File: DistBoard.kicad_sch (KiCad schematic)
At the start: 17 parts, among them J1 22-27-2021, J2 SSM-103-L-SV, J3 SSM-103-L-SV, J4 SSM-103-L-SV, J5 SSM-103-L-SV, U1 TLE2426CDR

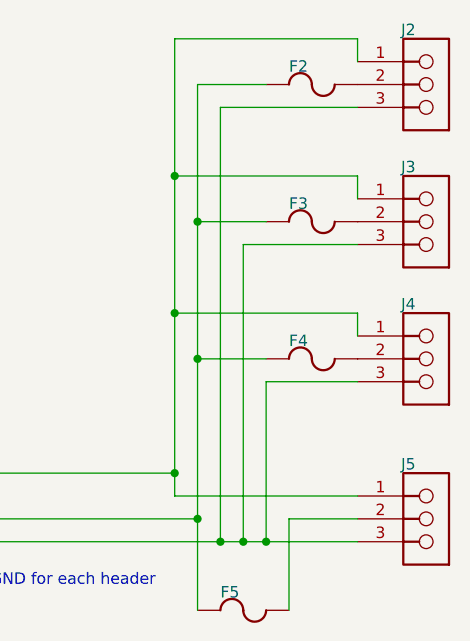
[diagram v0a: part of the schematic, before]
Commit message: Swap to through hole headers
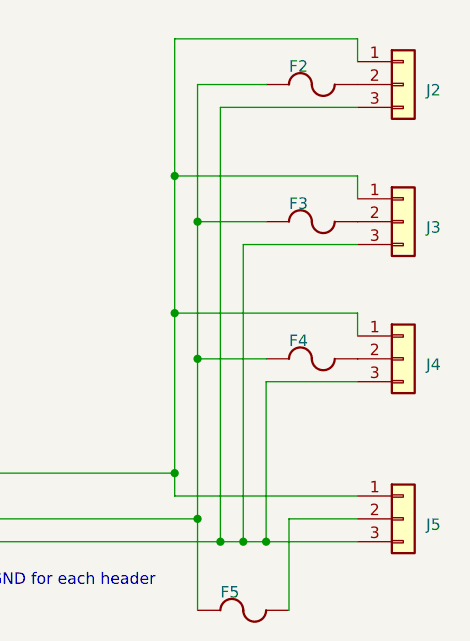
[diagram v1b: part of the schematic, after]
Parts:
- removed J2, J3, J4, J5: SSM-103-L-SV, SMTC-SSM-103-X-SV, symbol DistBoard-altium-import:root_3_SMTC-SSM-103-X-SV
- added J2, J3, J4, J5: Conn_01x03, Connector_PinHeader_2.54mm:PinHeader_1x03_P2.54mm_Vertical, symbol Connector_Generic:Conn_01x03
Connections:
- net AGND: now also J2.3 (Pin_3), J3.3 (Pin_3), J4.3 (Pin_3), J5.3 (Pin_3)
- net GND: now also J2.1 (Pin_1), J3.1 (Pin_1), J4.1 (Pin_1), J5.1 (Pin_1)
- net at F4.2: now also J4.2 (Pin_2)
- net at F5.2: now also J5.2 (Pin_2)
- net at F3.2: now also J3.2 (Pin_2)
- net at F2.2: now also J2.2 (Pin_2)

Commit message: Swap to socket headers and fix drc violations
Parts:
- J2, J3, J4, J5: footprint Connector_PinHeader_2.54mm:PinHeader_1x03_P2.54mm_Vertical -> Connector_PinSocket_2.54mm:PinSocket_1x03_P2.54mm_Vertical
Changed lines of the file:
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@@
       (effects (font (size 1.27 1.27)) (justify left) hide)
     )
-    (property "Footprint" "Connector_PinHeader_2.54mm:PinHeader_1x03_P2.54mm_Vertical" (at 203.2 104.14 0)
+    (property "Footprint" "Connector_PinSocket_2.54mm:PinSocket_1x03_P2.54mm_Vertical" (at 203.2 104.14 0)
       (effects (font (size 1.27 1.27)) hide)
     )
@@
       (effects (font (size 1.27 1.27)) (justify left) hide)
     )
-    (property "Footprint" "Connector_PinHeader_2.54mm:PinHeader_1x03_P2.54mm_Vertical" (at 203.2 137.16 0)
+    (property "Footprint" "Connector_PinSocket_2.54mm:PinSocket_1x03_P2.54mm_Vertical" (at 203.2 137.16 0)
       (effects (font (size 1.27 1.27)) hide)
     )
@@
       (effects (font (size 1.27 1.27)) (justify left) hide)
     )
-    (property "Footprint" "Connector_PinHeader_2.54mm:PinHeader_1x03_P2.54mm_Vertical" (at 203.2 88.9 0)
+    (property "Footprint" "Connector_PinSocket_2.54mm:PinSocket_1x03_P2.54mm_Vertical" (at 203.2 88.9 0)
       (effects (font (size 1.27 1.27)) hide)
     )
@@
       (effects (font (size 1.27 1.27)) (justify left) hide)
     )
-    (property "Footprint" "Connector_PinHeader_2.54mm:PinHeader_1x03_P2.54mm_Vertical" (at 203.2 119.38 0)
-      (effects (font (size 1.27 1.27)) hide)
-    )
+    (property "Footprint" "Connector_PinSocket_2.54mm:PinSocket_1x03_P2.54mm_Vertical" (at 203.2 119.38 0)
+      (effects (font (size 1.27 1.27)) hide)
+    )

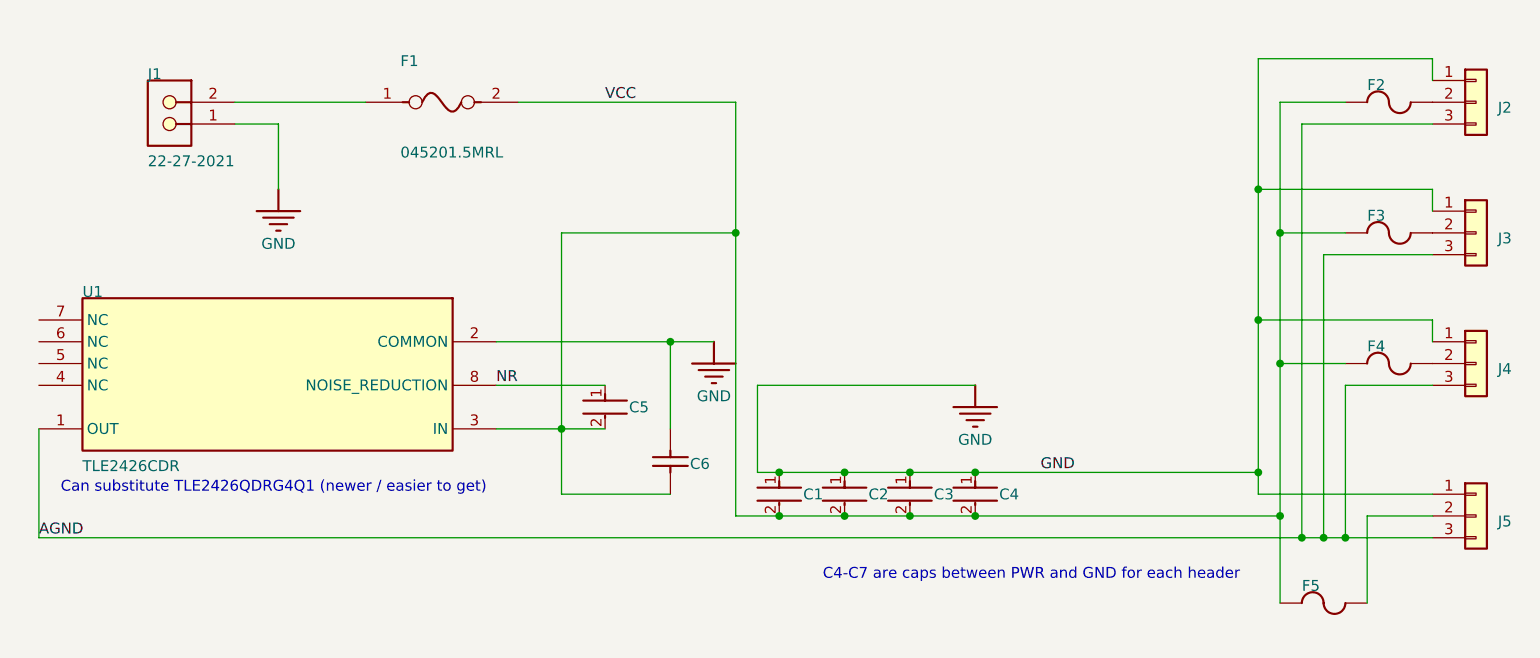
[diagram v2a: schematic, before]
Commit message: Schematic and BOM cleanup
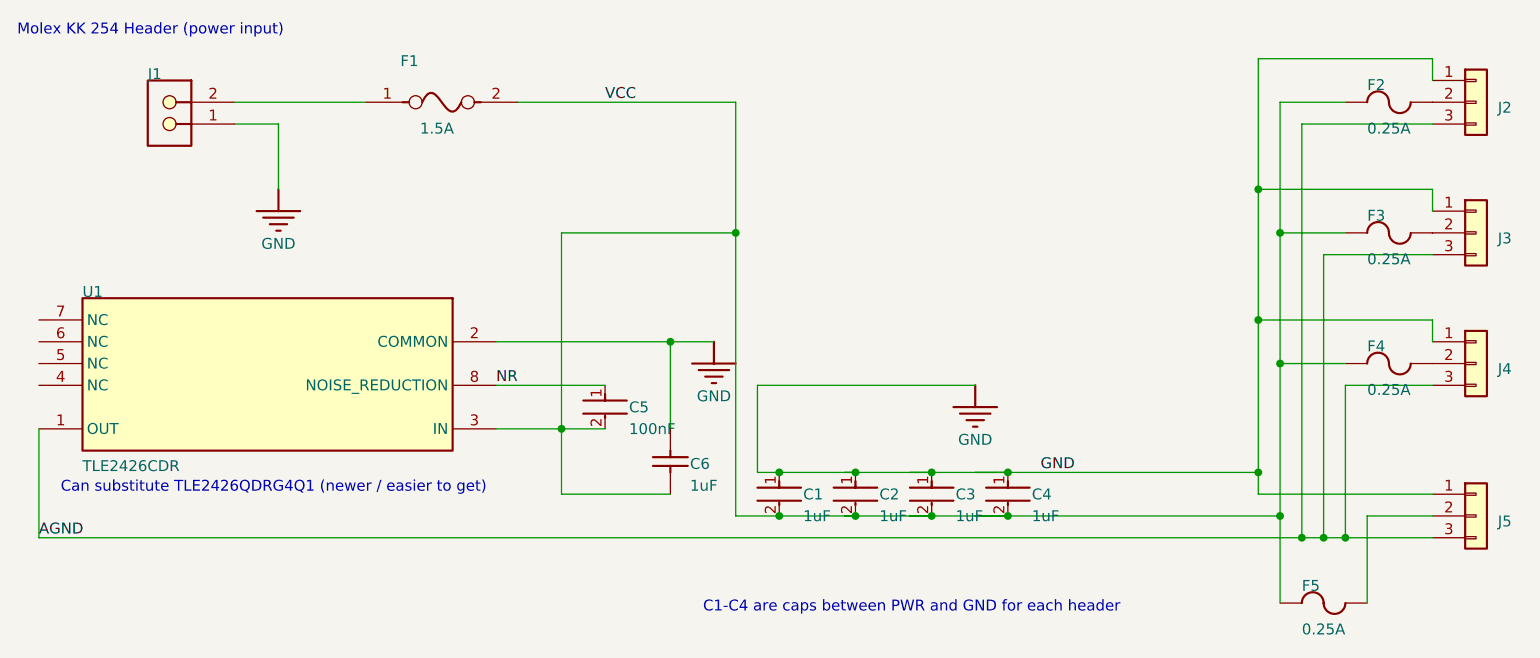
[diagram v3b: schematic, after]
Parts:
- C1, C2, C3, C4: value GCJ21BR71H105KA01L -> 1uF; footprint FP-GCJ21B-0_3-IPC_B -> Capacitor_SMD:C_0805_2012Metric_Pad1.18x1.45mm_HandSolder; ALTIUM_VALUE 1uF -> (none); Part Number (none) -> GCJ21BR71H105KA01L; WEIGHT 0.000335oz -> (none); WIDTH 0.049inch -> (none)
- C5: value GCD21BR71H104KA01L -> 100nF; footprint FP-GCD21B-0_15-IPC_C -> Capacitor_SMD:C_0805_2012Metric_Pad1.18x1.45mm_HandSolder; ALTIUM_VALUE 100nF -> (none); Part Number (none) -> GCD21BR71H104KA01L; WEIGHT 0.000335oz -> (none); WIDTH 0.049inch -> (none)
- C6: value C1206C105K5RACTU -> 1uF; footprint CAPC3216X110X50LL20T25 -> Capacitor_SMD:C_1206_3216Metric_Pad1.33x1.80mm_HandSolder; ALTIUM_UNNAMED_1 C1206C105K5RAC7800 -> (none); ALTIUM_VALUE 1uF -> (none); Part Number (none) -> C1206C105K5RACTU; VOLTAGE RATING DC 50V -> (none)
- F1: value 045201.5MRL -> 1.5A; ALTIUM_VALUE 0.093Ω -> (none); Part Number (none) -> 045201.5MRL
- F2, F3, F4, F5: value 0459.250UR -> 0.25A; Part Number (none) -> 0459.250UR; VOLTAGE RATING DC 125V -> (none)
- J1: Part Number (none) -> 22-27-2021
- U1: Part Number (none) -> TLE2426CDR; WEIGHT 0.002677oz -> (none); WIDTH 3.91mm -> (none)
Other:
- note added: "C1-C4 are caps between PWR and GND for each header"
- note added: "Molex KK 254 Header (power input)"
- note removed: "C4-C7 are caps between PWR and GND for each header"
- moved on the sheet: C2, C3, C4

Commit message: Fix schematic footprints not matching PCB
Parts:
- F1: footprint FP-0452-MFG -> AltiumImport:FP-0452-MFG
- F2, F3, F4, F5: footprint LFUS-459_V -> AltiumImport:LFUS-459_V
- J1: footprint MOLX-22-27-2021_V -> AltiumImport:MOLX-22-27-2021_V
- U1: footprint FP-D0008A-IPC_B -> AltiumImport:FP-D0008A-IPC_B
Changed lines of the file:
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@@
       (effects (font (size 1.27 1.27)) (justify left bottom))
     )
-    (property "Footprint" "FP-D0008A-IPC_B" (at 88.9 127 0)
+    (property "Footprint" "AltiumImport:FP-D0008A-IPC_B" (at 88.9 127 0)
       (effects (font (size 1.27 1.27)) hide)
     )
@@
       (effects (font (size 1.27 1.27)) (justify left bottom))
     )
-    (property "Footprint" "LFUS-459_V" (at 190.5 116.84 0)
+    (property "Footprint" "AltiumImport:LFUS-459_V" (at 190.5 116.84 0)
       (effects (font (size 1.27 1.27)) hide)
     )
@@
       (effects (font (size 1.27 1.27)) (justify left bottom))
     )
-    (property "Footprint" "LFUS-459_V" (at 190.5 101.6 0)
+    (property "Footprint" "AltiumImport:LFUS-459_V" (at 190.5 101.6 0)
       (effects (font (size 1.27 1.27)) hide)
     )
@@
       (effects (font (size 1.27 1.27)) (justify left bottom) hide)
     )
-    (property "Footprint" "MOLX-22-27-2021_V" (at 53.34 93.98 0)
+    (property "Footprint" "AltiumImport:MOLX-22-27-2021_V" (at 53.34 93.98 0)
       (effects (font (size 1.27 1.27)) hide)
     )
@@
       (effects (font (size 1.27 1.27)) (justify left bottom))
     )
-    (property "Footprint" "LFUS-459_V" (at 182.88 144.78 0)
+    (property "Footprint" "AltiumImport:LFUS-459_V" (at 182.88 144.78 0)
       (effects (font (size 1.27 1.27)) hide)
     )
@@
       (effects (font (size 1.27 1.27)) (justify left bottom))
     )
-    (property "Footprint" "LFUS-459_V" (at 190.5 86.36 0)
+    (property "Footprint" "AltiumImport:LFUS-459_V" (at 190.5 86.36 0)
       (effects (font (size 1.27 1.27)) hide)
     )
@@
       (effects (font (size 1.27 1.27)) (justify left bottom))
     )
-    (property "Footprint" "FP-0452-MFG" (at 73.66 88.9 0)
-      (effects (font (size 1.27 1.27)) hide)
-    )
+    (property "Footprint" "AltiumImport:FP-0452-MFG" (at 73.66 88.9 0)
+      (effects (font (size 1.27 1.27)) hide)
+    )

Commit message: Remove imported symbol table fiends
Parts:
- C1, C2, C3, C4: CAPACITANCE 1uF -> (none); CASE CODE (IMPERIAL) 0805 -> (none); CASE CODE (METRIC) 2012 -> (none); CASE/PACKAGE 0805 -> (none); DIELECTRIC X7R -> (none); FEATURES Soft Termination -> (none); HEIGHT 1.25mm -> (none); LEAD FREE Lead Free -> (none); LENGTH 0.079inch -> (none); MANUFACTURER Murata -> (none); MANUFACTURER PART NUMBER GCJ21BR71H105KA01L -> (none); MAX OPERATING TEMPERATURE 125°C -> (none); MIN OPERATING TEMPERATURE -55°C -> (none); MOUNT Surface Mount -> (none); PACKAGE QUANTITY 3000 -> (none); PACKAGING Tape and Reel -> (none); RATINGS AEC-Q200 -> (none); TERMINATION SMD/SMT -> (none); THICKNESS 0.057inch -> (none); TOLERANCE 10% -> (none); VOLTAGE RATING 50V -> (none); VOLTAGE RATING (DC) 50V -> (none)
- C5: CAPACITANCE 100nF -> (none); CASE CODE (IMPERIAL) 0805 -> (none); CASE CODE (METRIC) 2012 -> (none); CASE/PACKAGE 0805 -> (none); DEPTH 1.25mm -> (none); DIELECTRIC X7R -> (none); HEIGHT 1.25mm -> (none); LENGTH 2mm -> (none); MANUFACTURER Murata -> (none); MANUFACTURER PART NUMBER GCD21BR71H104KA01L -> (none); MAX OPERATING TEMPERATURE 125°C -> (none); MIN OPERATING TEMPERATURE -55°C -> (none); MOUNT Surface Mount -> (none); PACKAGE QUANTITY 3000 -> (none); PACKAGING Tape and Reel -> (none); RATINGS AEC-Q200 -> (none); TERMINATION SMD/SMT -> (none); THICKNESS 0.049inch -> (none); TOLERANCE 10% -> (none); VOLTAGE RATING 50V -> (none); VOLTAGE RATING (DC) 50V -> (none)
- C6: BRAND Kemet -> (none); CAPACITANCE 1uF -> (none); CAPACITANCE - NF 1000nF -> (none); CASE CODE - IN 1206 -> (none); CASE CODE - MM 3216 -> (none); CASE HEIGHT 1mm -> (none); CASE LENGTH 3.2mm -> (none); CASE WIDTH 1.6mm -> (none); CLASS Class1 -> (none); DATASHEET URL http://www.kemet.com/docfinder?Partnumber=C1206C105K5RACTU -> (none); DATASHEET VERSION 02/2016 -> (none); DIELECTRIC X7R -> (none); DIMENSIONS 1.6mmWx3.2mmLx1mmH -> (none); FACTORY PACK QUANTITY 2500 -> (none); MANUFACTURER Kemet -> (none); MANUFACTURER PART NUMBER C1206C105K5RACTU -> (none); MANUFACTURER URL http://www.kemet.com/ -> (none); MAXIMUM OPERATING TEMPERATURE +125C -> (none); MINIMUM OPERATING TEMPERATURE -55C -> (none); MOUNTING TECHNOLOGY SurfaceMount -> (none); OPERATING TEMPERATURE RANGE -55Cto+125C -> (none); PACKAGE / CASE 1206(3216metric) -> (none); PACKAGE DESCRIPTION 2-Pin Surface Mount Device, Body 3.2 x 1.6 mm -> (none); PACKAGE REFERENCE 1206 -> (none); PACKAGING Reel -> (none); PRICE 0.053 -> (none); PRODUCT GeneralTypeMLCCs -> (none); PRODUCT CATEGORY MultilayerCeramicCapacitorsMLCC-SMD/SMT -> (none); ROHS Details -> (none); SERIES C1206C -> (none); TEMPERATURE COEFFICIENT / CODE +/-15% -> (none); TERMINATION STYLE SMD/SMT -> (none); TOLERANCE 10% -> (none); TYPE SMDMLCCX7R6.3-250VDCCommericalGrade -> (none); VOLTAGE RATING 50V -> (none)
- F1: AUTOMOTIVE No -> (none); CATEGORY Fuse -> (none); COMPONENTLINK2DESCRIPTION Datasheet -> (none); COMPONENTLINK2URL https://www.littelfuse.com/~/media/electronics/datasheets/f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 -> (none); DEVICE CLASS L1 Circuit Protection -> (none); DEVICE CLASS L2 Fuses -> (none); DEVICE CLASS L3 unset -> (none); DIGIKEY DESCRIPTION FUSE BRD MNT 1.5A 125VAC/VDC SMD -> (none); FUSE BLOW SPEED Slow -> (none); FUSE CURRENT 1.5A -> (none); FUSE I2T 3.65A2Sec -> (none); FUSE INTERRUPT AC CURRENT 50A -> (none); FUSE INTERRUPT DC CURRENT 300A -> (none); HEIGHT 2.94mm -> (none); LEAD FREE Yes -> (none); MANUFACTURER Littelfuse Inc -> (none); MANUFACTURER PART NUMBER 045201.5MRL -> (none); MAX FUSE AC VOLTAGE 125V -> (none); MAX FUSE DC VOLTAGE 125V -> (none); MOUSER DESCRIPTION Surface Mount Fuses 125V 1.5A -> (none); OCTOPART https://octopart.com/045201.5mrl-littelfuse-566412 -> (none); PACKAGE 0452 -> (none); RESISTANCE 0.093Ω -> (none); ROHS TRUE -> (none); TEMPERATURE -55°C to +125°C -> (none); TEMPERATURE RANGE HIGH +125°C -> (none); TEMPERATURE RANGE LOW -55°C -> (none); VOLTAGE RATING 125V -> (none)
- F2, F3, F4, F5: BRAND Littelfuse -> (none); CASE HEIGHT 3.05mm -> (none); CASE LENGTH 7.24mm -> (none); CASE WIDTH 4.32mm -> (none); CURRENT RATING 250mA -> (none); DATASHEET URL http://www.littelfuse.com/~/media/electronics/datasheets/fu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 -> (none); DATASHEET VERSION 11/2015 -> (none); DIMENSIONS 7.24mmLx4.32mmW -> (none); FACTORY PACK QUANTITY 500 -> (none); FUSE SIZE / GROUP PICO -> (none); FUSE TYPE FastBlow -> (none); INTERRUPT RATING 300Amps -> (none); MANUFACTURER Littelfuse -> (none); MANUFACTURER PART NUMBER 0459.250UR -> (none); MANUFACTURER URL http://www.littelfuse.com/ -> (none); MOUNTING TECHNOLOGY SurfaceMount -> (none); OPERATING TEMPERATURE RANGE -55Cto+125C -> (none); PACKAGE DESCRIPTION 2-Pin Surface Mount Device, Body 7.24 x 4.32 mm -> (none); PACKAGE REFERENCE 459 -> (none); PACKAGING Reel -> (none); PRODUCT SurfaceMountFuses -> (none); PRODUCT CATEGORY SurfaceMountFuses -> (none); PRODUCT TYPE SurfaceMountFuse -> (none); RESISTANCE 665mOhms -> (none); ROHS Details -> (none); SERIES 459 -> (none); TYPE PicoSurfaceMountVeryFastActingFuse -> (none)
- J1: CONTACT MATERIAL Tinplatedbrass -> (none); CURRENT - MAX 4A -> (none); CURRENT RATING 4A -> (none); DATASHEET URL http://www.molex.com/pdm_docs/sd/022272021_sd.pdf -> (none); DATASHEET VERSION Rev. F, 06/2009 -> (none); HOUSING MATERIAL Nylon(UL94V-0) -> (none); MANUFACTURER Molex -> (none); MANUFACTURER PART NUMBER 22-27-2021 -> (none); MANUFACTURER URL http://www.molex.com/ -> (none); MOUNTING TECHNOLOGY ThroughHole -> (none); NO. OF POSITIONS 2 -> (none); NO. OF ROWS 1 -> (none); OPERATING TEMPERATURE 0°Cto+75°C -> (none); ORIENTATION Vertical -> (none); PACKAGE DESCRIPTION 2-Leads Header, Body 5.08 x 5.8 mm, Pitch 2.54 mm -> (none); PACKAGE REFERENCE 22-27-2021 -> (none); PACKAGE VERSION Rev. BC, 02/2012 -> (none); PARTNUMBER 0022272021 -> (none); PITCH 2.54mm -> (none); VOLTAGE - MAX 250V -> (none); VOLTAGE RATING 250V -> (none)
- U1: CASE/PACKAGE SOIC -> (none); HEIGHT 1.58mm -> (none); LEAD FREE Lead Free -> (none); LENGTH 4.9mm -> (none); MANUFACTURER Texas Instruments -> (none); MANUFACTURER PART NUMBER TLE2426CDR -> (none); MAX INPUT VOLTAGE 40V -> (none); MAX OPERATING TEMPERATURE 125°C -> (none); MAX OUTPUT CURRENT 20mA -> (none); MAX OUTPUT VOLTAGE 20V -> (none); MIN OPERATING TEMPERATURE -55°C -> (none); MIN OUTPUT VOLTAGE 2V -> (none); MOUNT Surface Mount -> (none); NUMBER OF PINS 8 -> (none); OPERATING SUPPLY CURRENT 400uA -> (none); OUTPUT CURRENT 20mA -> (none); OUTPUT TYPE Adjustable -> (none); OUTPUT VOLTAGE 20V -> (none); PACKAGE QUANTITY 1 -> (none); PACKAGING Tape and Reel -> (none); RADIATION HARDENING No -> (none); REACH SVHC No SVHC -> (none); REFERENCE TYPE Ground Reference (Virtual) -> (none); REFERENCE VOLTAGE 20V -> (none); TEMPERATURE COEFFICIENT 35ppm/°C -> (none); TOLERANCE 1% -> (none)
